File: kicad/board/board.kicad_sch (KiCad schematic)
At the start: 41 parts

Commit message: wired up and imported
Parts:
- added JST1, JST2: Conn_01x02, symbol Connector_Generic:Conn_01x02
- added S19: SSSS811101, SSSS811101:SW_SSSS811101, symbol cSWITCH:SSSS811101
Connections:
- net at D10.1 (K): now also S10.1 (A); no longer S10.2 (B)
- net G2: now reaches D10.2 (A)
- net G2: now also D1.2 (A), D13.2 (A), D4.2 (A), D7.2 (A), U1.8 (P8)
- net at S18.1 (A): now also D18.1 (K)
- net C4: now reaches S18.2 (B)
- net C4: now also S13.2 (B), S14.2 (B), S15.2 (B), U1.4 (P4); no longer D18.1 (K)
- net at D14.1 (K): now also S14.1 (A); no longer S14.2 (B)
- net G1: now reaches D14.2 (A)
- net G1: now also D11.2 (A), D2.2 (A), D5.2 (A), D8.2 (A), U1.9 (P9)
- net C0: now reaches U1.0 (P0)
- net C0: now also S1.2 (B), S2.2 (B), S3.2 (B)
- net C1: now reaches U1.1 (P1)
- net C1: now also S4.2 (B), S5.2 (B), S6.2 (B)
- net G0: now reaches U1.10 (P10)
- net G0: now also D12.2 (A), D15.2 (A), D3.2 (A), D6.2 (A), D9.2 (A)
- net C2: now reaches U1.2 (P2)
- net C2: now also S16.2 (B), S7.2 (B), S8.2 (B), S9.2 (B)
- net C3: now reaches U1.3 (P3)
- net C3: now also S10.2 (B), S11.2 (B), S12.2 (B), S17.2 (B)
- net G3: now reaches U1.7 (P7)
- net G3: now also D16.2 (A), D17.2 (A), D18.2 (A)
- net at D8.1 (K): now also S8.1 (A); no longer S8.2 (B)
- net at S1.1 (A): now also D1.1 (K)
- net at S17.1 (A): now also D17.1 (K)
- net at S4.1 (A): now also D4.1 (K)
- net at S3.1 (A): now also D3.1 (K)
- net at D13.1 (K): now also S13.1 (A); no longer S13.2 (B)
- net at S7.1 (A): now also D7.1 (K)
- net at D15.1 (K): now also S15.1 (A); no longer S15.2 (B)
- net at D5.1 (K): now also S5.1 (A); no longer S5.2 (B)
- net at D2.1 (K): now also S2.1 (A); no longer S2.2 (B)
- net at D12.1 (K): now also S12.1 (A); no longer S12.2 (B)
- net at S16.1 (A): now also D16.1 (K)
- net at D11.1 (K): now also S11.1 (A); no longer S11.2 (B)
- net at S6.1 (A): now also D6.1 (K)
- net at S9.1 (A): now also D9.1 (K)
- new net: JST1.1 (Pin_1), S19.2
- new net: JST1.2 (Pin_2), JST2.1 (Pin_1)
- new net: JST2.2 (Pin_2), S19.3
- no-connect marks 0 -> 6
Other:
- moved on the sheet: D1, D10, D11, D12, D13, D14, D15, D16, D17, D18, D2, D3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

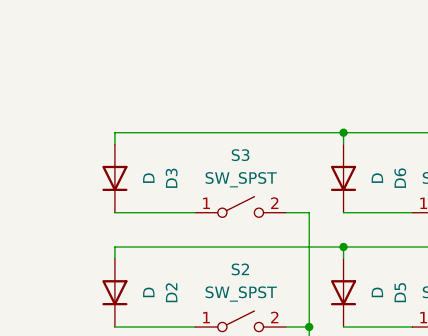
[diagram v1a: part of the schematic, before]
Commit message: fixed footprints
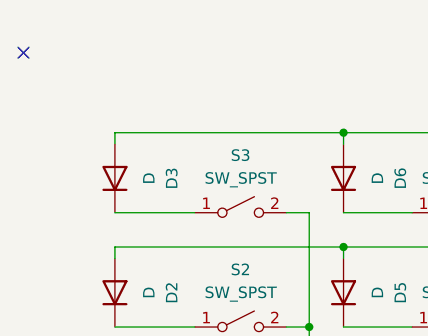
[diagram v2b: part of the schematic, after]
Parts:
- D12: footprint (none) -> clacken:reversable_diode
- H1, H2, H3, H4: footprint (none) -> MountingHole:MountingHole_2.2mm_M2
- JST1, JST2: footprint (none) -> clacken:JST_angled
- S19: footprint SSSS811101:SW_SSSS811101 -> sCLACKEN:SW_SSSS811101
- U1: footprint (none) -> clacken:seeed_xaio
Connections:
- no-connect marks 6 -> 7
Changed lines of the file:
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@@
 	)
 	(no_connect
+		(at 27.94 33.02)
+	)
+	(no_connect
 		(at 203.2 40.64)
 	)
@@
 			)
 		)
-		(property "Footprint" ""
+		(property "Footprint" "MountingHole:MountingHole_2.2mm_M2"
 			(at 157.48 193.04 0)
 			(effects
@@
 			)
 		)
-		(property "Footprint" ""
+		(property "Footprint" "clacken:seeed_xaio"
 			(at 195.58 45.72 0)
 			(effects
@@
 			)
 		)
-		(property "Footprint" ""
+		(property "Footprint" "clacken:JST_angled"
 			(at 191.77 69.85 0)
 			(effects
@@
 			)
 		)
-		(property "Footprint" ""
+		(property "Footprint" "MountingHole:MountingHole_2.2mm_M2"
 			(at 138.43 186.69 0)
 			(effects
@@
 			)
 		)
-		(property "Footprint" ""
+		(property "Footprint" "MountingHole:MountingHole_2.2mm_M2"
 			(at 157.48 186.69 0)
 			(effects
@@
 			)
 		)
-		(property "Footprint" ""
+		(property "Footprint" "clacken:reversable_diode"
 			(at 114.3 46.99 0)
 			(effects
@@
 			)
 		)
-		(property "Footprint" ""
+		(property "Footprint" "clacken:JST_angled"
 			(at 207.01 67.31 0)
 			(effects
@@
 			)
 		)
-		(property "Footprint" ""
+		(property "Footprint" "MountingHole:MountingHole_2.2mm_M2"
 			(at 138.43 193.04 0)
 			(effects
@@
 			)
 		)
-		(property "Footprint" "SSSS811101:SW_SSSS811101"
+		(property "Footprint" "sCLACKEN:SW_SSSS811101"
 			(at 198.12 87.63 0)
 			(effects

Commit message: we messed up pcb
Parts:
- added S20: SSSS811101, sCLACKEN:SW_SSSS811101, symbol cSWITCH:SSSS811101
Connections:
- net C0: now also U1.2 (P2); no longer U1.0 (P0)
- net C1: now also U1.3 (P3); no longer U1.1 (P1)
- net C2: now also U1.4 (P4); no longer U1.2 (P2)
- net C3: now also U1.5 (P5); no longer U1.3 (P3)
- net C4: now also U1.6 (P6); no longer U1.4 (P4)
- net G0: now also D12.1 (K), D15.1 (K), D3.1 (K), D6.1 (K), D9.1 (K); no longer D12.2 (A), D15.2 (A), D3.2 (A), D6.2 (A), D9.2 (A)
- net G1: now also D11.1 (K), D14.1 (K), D2.1 (K), D5.1 (K), D8.1 (K); no longer D11.2 (A), D14.2 (A), D2.2 (A), D5.2 (A), D8.2 (A)
- net G2: now also D1.1 (K), D10.1 (K), D13.1 (K), D4.1 (K), D7.1 (K); no longer D1.2 (A), D10.2 (A), D13.2 (A), D4.2 (A), D7.2 (A)
- net G3: now also D16.1 (K), D17.1 (K), D18.1 (K); no longer D16.2 (A), D17.2 (A), D18.2 (A)
- net at S10.1 (A): now also D10.2 (A); no longer D10.1 (K)
- net at S18.1 (A): now also D18.2 (A); no longer D18.1 (K)
- net at S14.1 (A): now also D14.2 (A); no longer D14.1 (K)
- net at S8.1 (A): now also D8.2 (A); no longer D8.1 (K)
- net at S1.1 (A): now also D1.2 (A); no longer D1.1 (K)
- net at S17.1 (A): now also D17.2 (A); no longer D17.1 (K)
- net at S4.1 (A): now also D4.2 (A); no longer D4.1 (K)
- net at S3.1 (A): now also D3.2 (A); no longer D3.1 (K)
- net at JST1.1 (Pin_1), S19.2: now also S20.2
- net at S13.1 (A): now also D13.2 (A); no longer D13.1 (K)
- net at S7.1 (A): now also D7.2 (A); no longer D7.1 (K)
- net at S15.1 (A): now also D15.2 (A); no longer D15.1 (K)
- net at S5.1 (A): now also D5.2 (A); no longer D5.1 (K)
- net at S2.1 (A): now also D2.2 (A); no longer D2.1 (K)
- net at S12.1 (A): now also D12.2 (A); no longer D12.1 (K)
- net at JST2.2 (Pin_2), S19.3: now also S20.1
- net at S16.1 (A): now also D16.2 (A); no longer D16.1 (K)
- net at S11.1 (A): now also D11.2 (A); no longer D11.1 (K)
- net at S6.1 (A): now also D6.2 (A); no longer D6.1 (K)
- net at S9.1 (A): now also D9.2 (A); no longer D9.1 (K)
- no-connect marks 7 -> 8
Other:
- moved on the sheet: D1, D10, D11, D12, D13, D14, D15, D16, D17, D18, D2, D3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
